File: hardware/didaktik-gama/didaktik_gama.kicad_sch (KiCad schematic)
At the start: 203 parts, among them J1 Klávesnice, J2 MG, J3 TV, J4 Porty 8255, J5 Napájení 9–12V DC, J6 Video (cinch), SW1 RESET, T1 KSY72, T2 KSY72, T3 KC507, T4 KC507 (BC547), T5 KC507 (Sp TR1 ZTX313), T6 KC507 (Sp TR2 ZTX313), T7 KF517 (Sp TR5 ZTX213), T8 KD139 (Sp TR4 ZTX651/TIP31), U1 UA880D (Z80), U10 4164, U11 4164, U12 4164, U13 4164, U14 4164, U15 4164, U16 4164, U17 2118, U18 2118, U19 2118, U2 27128 (16K EPROM), U20 2118, U21 2118, U22 2118, U23 2118, U24 2118, U25 74LS04, U26 74LS04, U27 74LS00, U28 74LS10, U29 74LS32, U3 8255 (MHB8255), U30 LM1889N, U31 VF modulátor (UM1233 nebo ekv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, U32 MA7805, U4 ULA, U5 74LS157, U6 74LS157, U7 74LS157, U8 74LS157, U9 4164, Y1 14MHz, Y2 4.433619MHz (Sp X2)

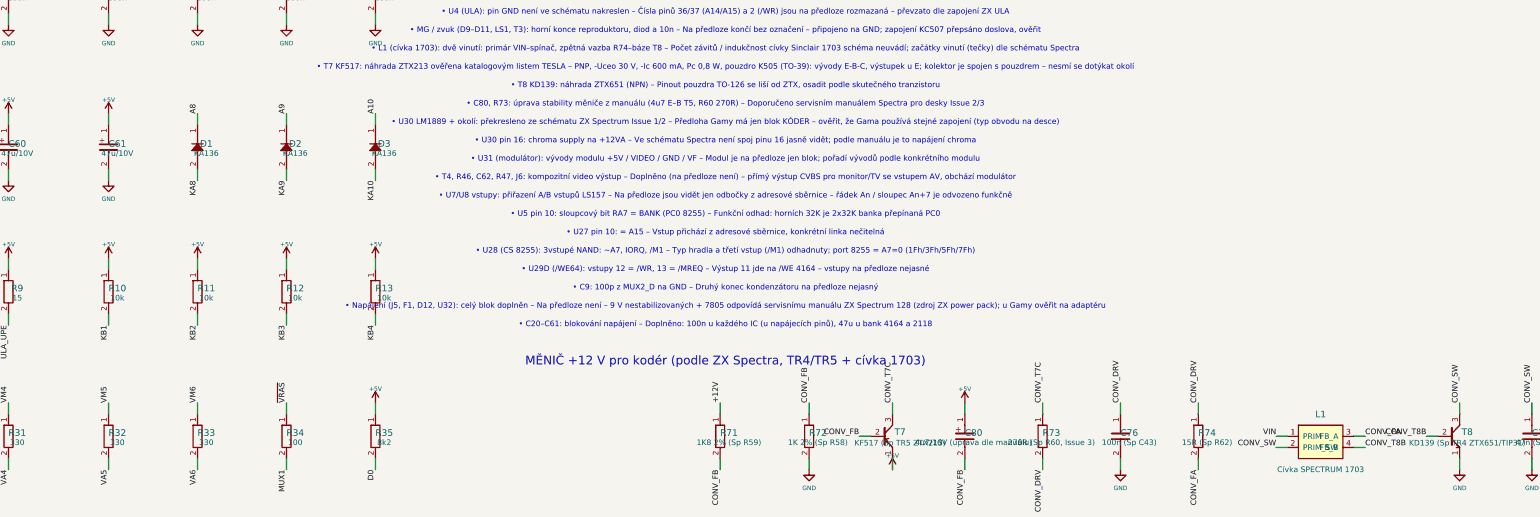
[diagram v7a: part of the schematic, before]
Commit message: Use TO-126 E-C-B pin order for KD139 (T8), confirm it from TESLA datasheet
Co-Authored-By: Claude Opus 5.5 <noreply@anthropic.com>
Claude-Session: https://claude.ai/code/session_01LAVM7Gq9EYiUXiCEdy9ZRx
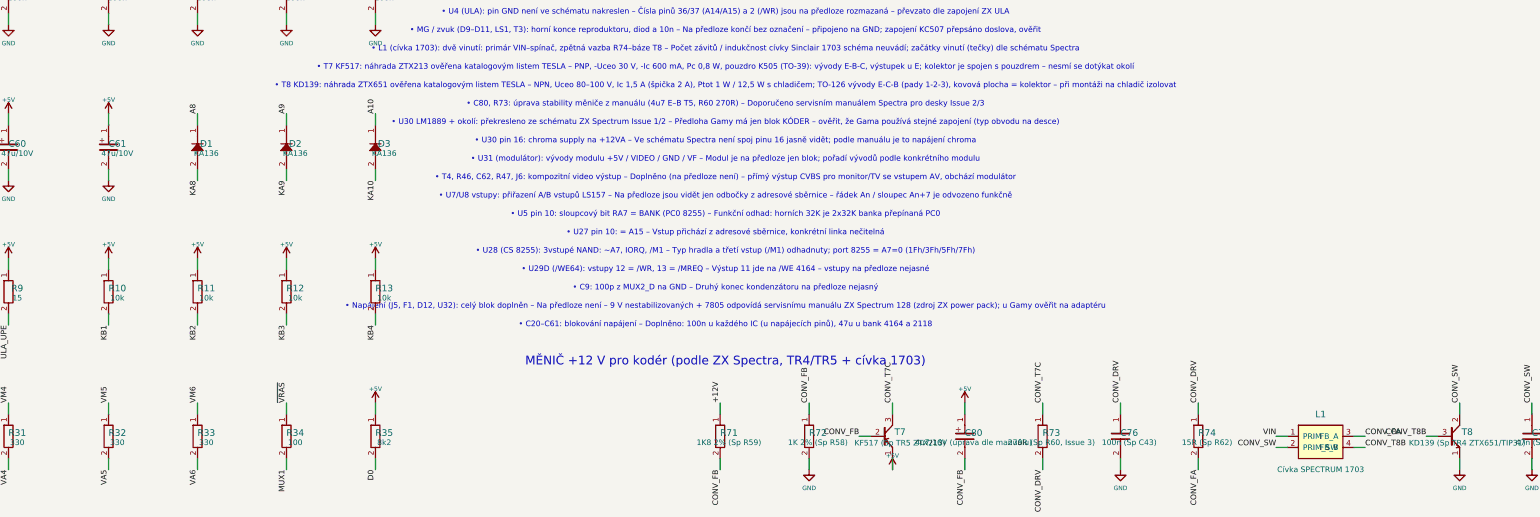
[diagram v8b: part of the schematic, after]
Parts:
- T8: symbol gama:NPN -> gama:NPN_ECB
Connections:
- net CONV_SW: now also T8.2 (C); no longer T8.3 (C)
- net CONV_T8B: now also T8.3 (B); no longer T8.2 (B)
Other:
- note added: "• T8 KD139: náhrada ZTX651 ověřena katalogovým listem TESLA – NPN, Uceo 80–100 V, Ic 1,5 A (špička 2 A), Ptot 1 W / 12,5 W s chladičem; TO-126 vývody E-C-B (pady 1-2-3), kovová plocha = kolektor – při montáži na chladič izolovat"
- note removed: "• T8 KD139: náhrada ZTX651 (NPN) – Pinout pouzdra TO-126 se liší od ZTX, osadit podle skutečného tranzistoru"
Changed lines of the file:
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@@
         (size 1.27 1.27)))
 )
-  (text "• T8 KD139: náhrada ZTX651 (NPN) – Pinout pouzdra TO-126 se liší od ZTX, osadit podle skutečného tranzistoru"
+  (text "• T8 KD139: náhrada ZTX651 ověřena katalogovým listem TESLA – NPN, Uceo 80–100 V, Ic 1,5 A (špička 2 A), Ptot 1 W / 12,5 W s chladičem; TO-126 vývody E-C-B (pady 1-2-3), kovová plocha = kolektor – při montáži na chladič izolovat"
     (at 560.00 339.00 0)
     (effects
@@
         (path "/749bded9-dac2-5d4c-8e6d-156d036e5f62" (reference "L1") (unit 1)))))
   (symbol
-    (lib_id "gama:NPN")
+    (lib_id "gama:NPN_ECB")
     (at 726.44 419.10 0)
     (unit 1)
